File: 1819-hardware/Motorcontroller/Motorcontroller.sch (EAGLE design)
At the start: 33 parts, among them U1 GENERIC-SOIC8MSGEQ7N-FILTER, U2 GENERIC-SOIC8MSGEQ7N-FILTER, U3 GENERIC-SOIC8MSGEQ7N-FILTER

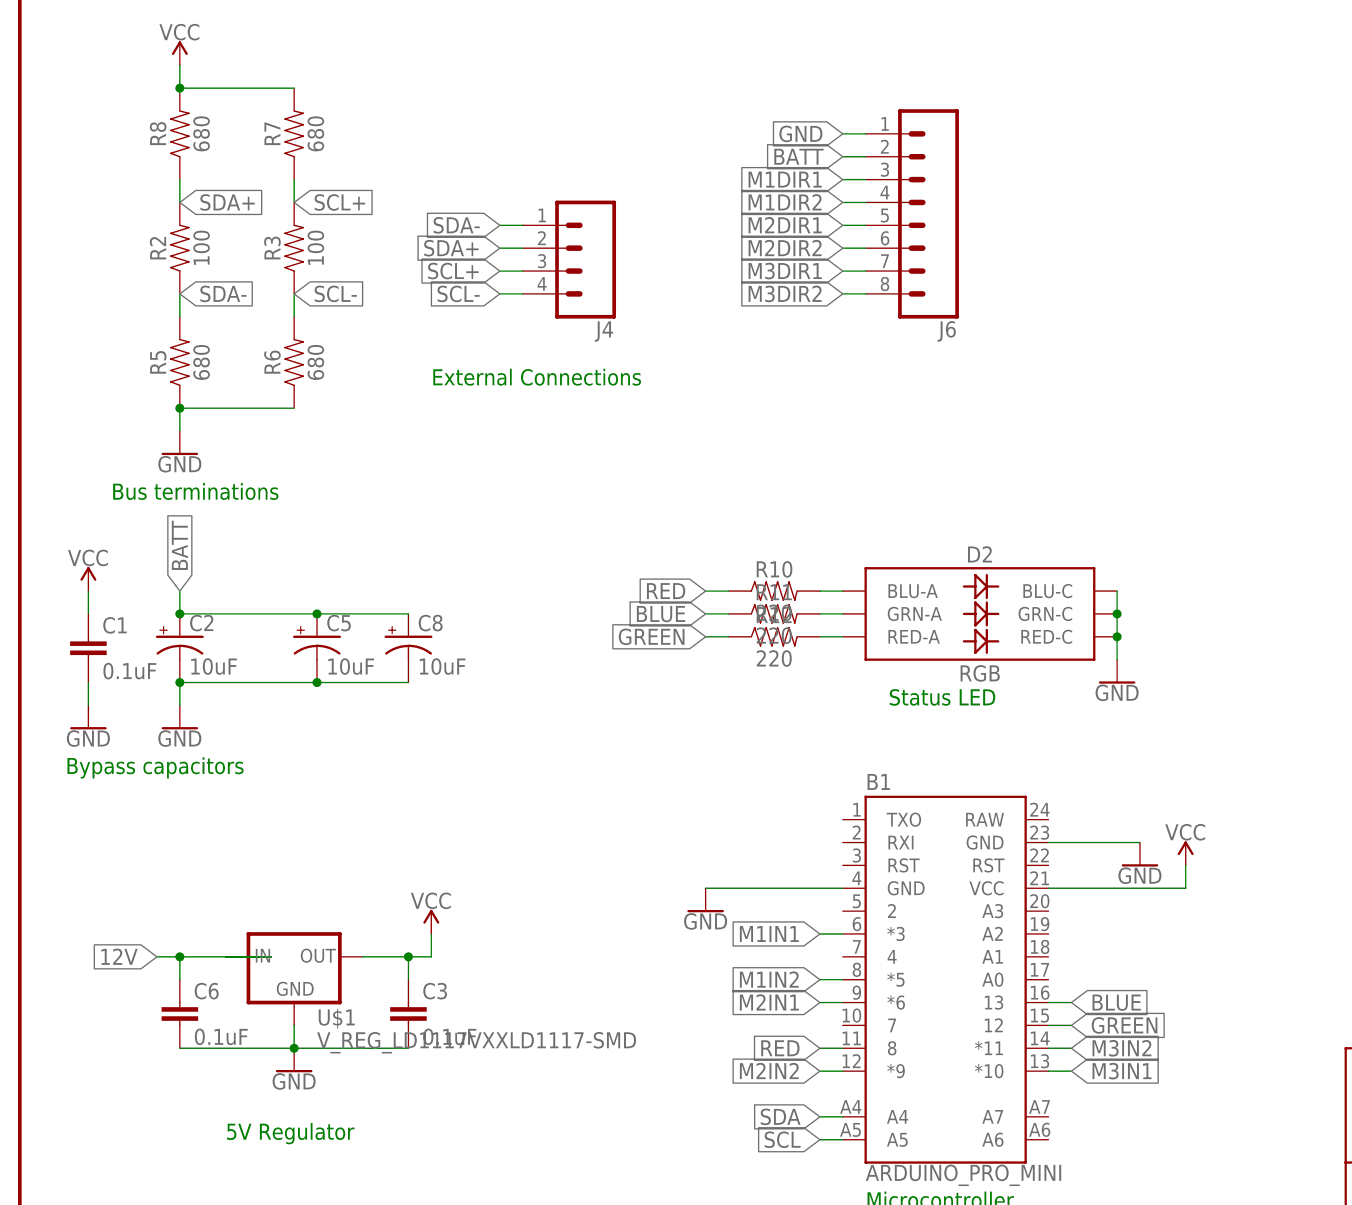
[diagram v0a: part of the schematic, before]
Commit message: routing of motorcontroller board files
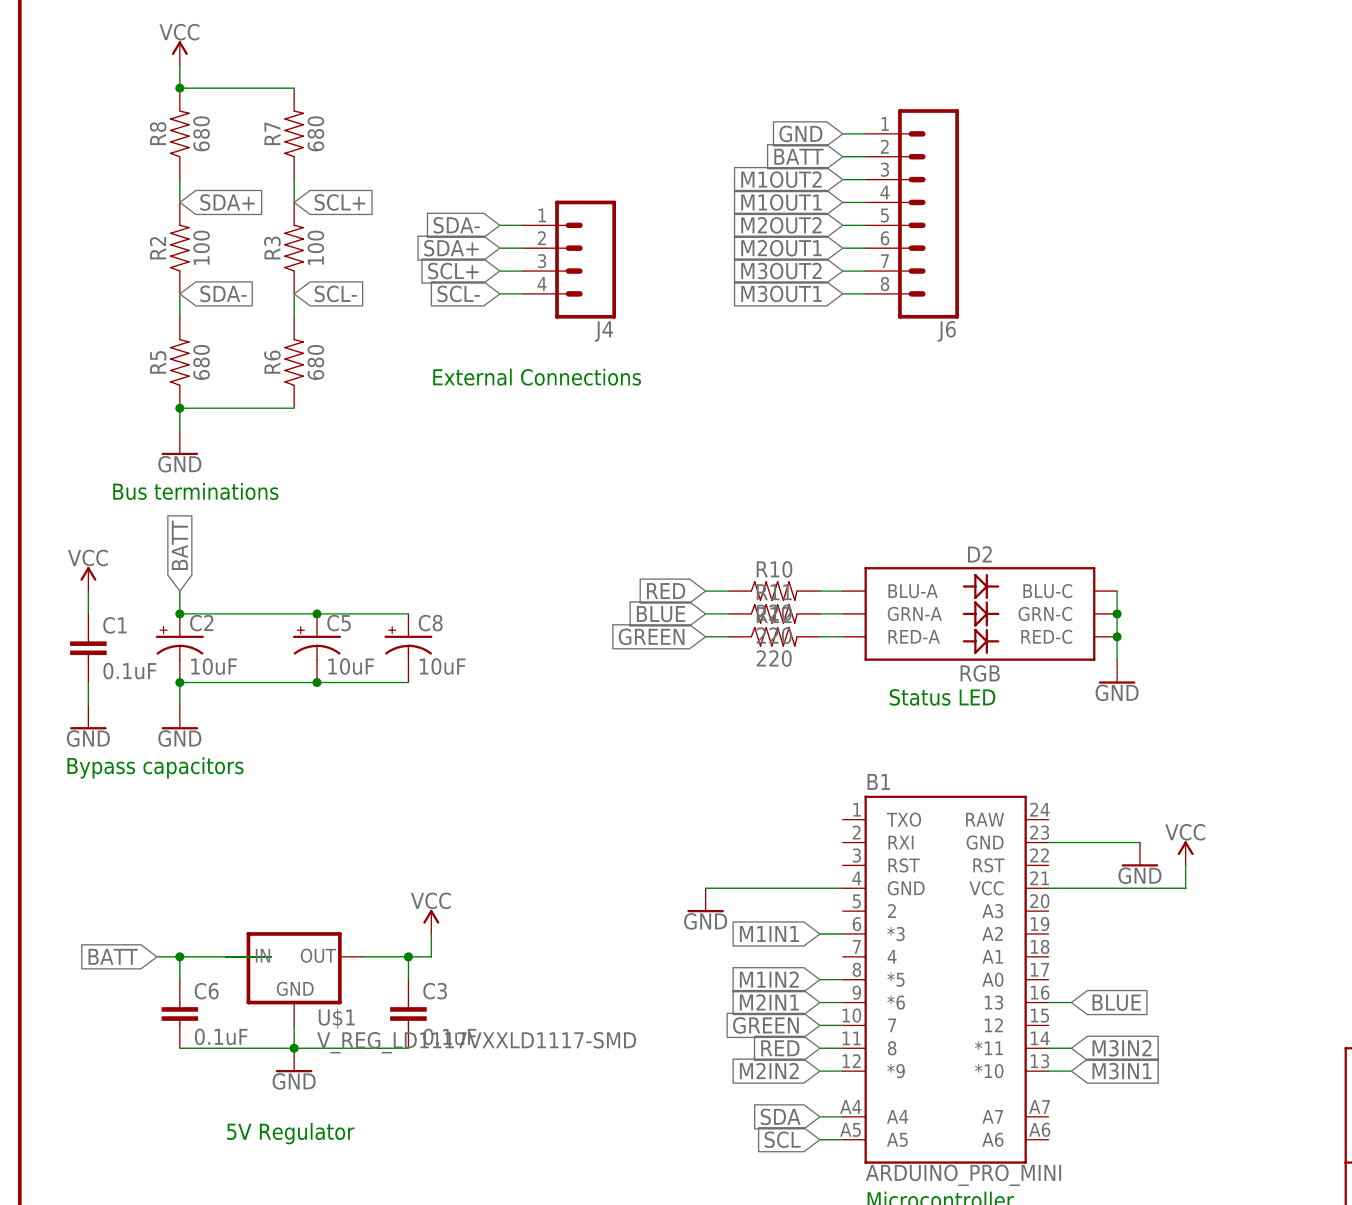
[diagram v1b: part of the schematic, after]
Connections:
- removed net 12V: C6.1, U$1.IN
- removed net M1DIR1: J6.3
- removed net M1DIR2: J6.4
- removed net M2DIR1: J6.5
- removed net M2DIR2: J6.6
- removed net M3DIR1: J6.7
- removed net M3DIR2: J6.8
- net BATT: now also C6.1, U$1.IN
- net GREEN: now also B1.7; no longer B1.12
- net M1OUT1: now also J6.4
- net M1OUT2: now also J6.3
- net M2OUT1: now also J6.6
- net M2OUT2: now also J6.5
- net M3OUT1: now also J6.8
- net M3OUT2: now also J6.7
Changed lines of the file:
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@@
-</segment>
-</net>
-<net name="12V" class="0">
-<segment>
-<pinref part="U$1" gate="G$1" pin="IN"/>
-<wire x1="22.86" y1="45.72" x2="27.94" y2="45.72" width="0.1524" layer="91"/>
-<wire x1="27.94" y1="45.72" x2="17.78" y2="45.72" width="0.1524" layer="91"/>
-<pinref part="C6" gate="G$1" pin="1"/>
-<wire x1="17.78" y1="45.72" x2="17.78" y2="43.18" width="0.1524" layer="91"/>
-<wire x1="17.78" y1="45.72" x2="15.24" y2="45.72" width="0.1524" layer="91"/>
-<junction x="17.78" y="45.72"/>
-<label x="15.24" y="45.72" size="1.778" layer="95" rot="R180" xref="yes"/>
 </segment>
 </net>
@@
 <net name="GREEN" class="0">
 <segment>
-<pinref part="B1" gate="G$1" pin="12"/>
-<wire x1="114.3" y1="38.1" x2="116.84" y2="38.1" width="0.1524" layer="91"/>
-<label x="116.84" y="38.1" size="1.778" layer="95" xref="yes"/>
-</segment>
-<segment>
 <pinref part="R12" gate="G$1" pin="1"/>
 <wire x1="78.74" y1="81.28" x2="76.2" y2="81.28" width="0.1524" layer="91"/>
 <label x="76.2" y="81.28" size="1.778" layer="95" rot="R180" xref="yes"/>
+</segment>
+<segment>
+<pinref part="B1" gate="G$1" pin="7"/>
+<wire x1="91.44" y1="38.1" x2="88.9" y2="38.1" width="0.1524" layer="91"/>
+<label x="88.9" y="38.1" size="1.778" layer="95" rot="R180" xref="yes"/>
 </segment>
 </net>
@@
 <label x="17.78" y="86.36" size="1.778" layer="95" rot="R90" xref="yes"/>
 </segment>
+<segment>
+<pinref part="U$1" gate="G$1" pin="IN"/>
+<wire x1="22.86" y1="45.72" x2="27.94" y2="45.72" width="0.1524" layer="91"/>
+<wire x1="27.94" y1="45.72" x2="17.78" y2="45.72" width="0.1524" layer="91"/>
+<pinref part="C6" gate="G$1" pin="1"/>
+<wire x1="17.78" y1="45.72" x2="17.78" y2="43.18" width="0.1524" layer="91"/>
+<wire x1="17.78" y1="45.72" x2="15.24" y2="45.72" width="0.1524" layer="91"/>
+<junction x="17.78" y="45.72"/>
+<label x="15.24" y="45.72" size="1.778" layer="95" rot="R180" xref="yes"/>
+</segment>
 </net>
 <net name="M1IN1" class="0">
@@
 <label x="198.12" y="167.64" size="1.778" layer="95" xref="yes"/>
 </segment>
+<segment>
+<pinref part="J6" gate="G$1" pin="3"/>
+<wire x1="93.98" y1="132.08" x2="91.44" y2="132.08" width="0.1524" layer="91"/>
+<label x="91.44" y="132.08" size="1.778" layer="95" rot="R180" xref="yes"/>
+</segment>
 </net>
 <net name="M1OUT1" class="0">
@@
 <label x="198.12" y="162.56" size="1.778" layer="95" xref="yes"/>
 </segment>
+<segment>
+<pinref part="J6" gate="G$1" pin="4"/>
+<wire x1="93.98" y1="129.54" x2="91.44" y2="129.54" width="0.1524" layer="91"/>
+<label x="91.44" y="129.54" size="1.778" layer="95" rot="R180" xref="yes"/>
+</segment>
 </net>
 <net name="N$1" class="0">
@@
 <label x="198.12" y="124.46" size="1.778" layer="95" xref="yes"/>
 </segment>
+<segment>
+<pinref part="J6" gate="G$1" pin="5"/>
+<wire x1="93.98" y1="127" x2="91.44" y2="127" width="0.1524" layer="91"/>
+<label x="91.44" y="127" size="1.778" layer="95" rot="R180" xref="yes"/>
+</segment>
 </net>
 <net name="M2OUT1" class="0">
@@
 <label x="198.12" y="119.38" size="1.778" layer="95" xref="yes"/>
 </segment>
+<segment>
+<pinref part="J6" gate="G$1" pin="6"/>
+<wire x1="93.98" y1="124.46" x2="91.44" y2="124.46" width="0.1524" layer="91"/>
+<label x="91.44" y="124.46" size="1.778" layer="95" rot="R180" xref="yes"/>
+</segment>
 </net>
 <net name="M3OUT2" class="0">
@@
 <label x="198.12" y="78.74" size="1.778" layer="95" xref="yes"/>
 </segment>
+<segment>
+<pinref part="J6" gate="G$1" pin="7"/>
+<wire x1="93.98" y1="121.92" x2="91.44" y2="121.92" width="0.1524" layer="91"/>
+<label x="91.44" y="121.92" size="1.778" layer="95" rot="R180" xref="yes"/>
+</segment>
 </net>
 <net name="M3OUT1" class="0">
@@
 <label x="198.12" y="73.66" size="1.778" layer="95" xref="yes"/>
 </segment>
-</net>
-<net name="M1DIR1" class="0">
-<segment>
-<pinref part="J6" gate="G$1" pin="3"/>
-<wire x1="93.98" y1="132.08" x2="91.44" y2="132.08" width="0.1524" layer="91"/>
-<label x="91.44" y="132.08" size="1.778" layer="95" rot="R180" xref="yes"/>
-</segment>
-</net>
-<net name="M1DIR2" class="0">
-<segment>
-<pinref part="J6" gate="G$1" pin="4"/>
-<wire x1="93.98" y1="129.54" x2="91.44" y2="129.54" width="0.1524" layer="91"/>
-<label x="91.44" y="129.54" size="1.778" layer="95" rot="R180" xref="yes"/>
-</segment>
-</net>
-<net name="M2DIR1" class="0">
-<segment>
-<pinref part="J6" gate="G$1" pin="5"/>
-<wire x1="93.98" y1="127" x2="91.44" y2="127" width="0.1524" layer="91"/>
-<label x="91.44" y="127" size="1.778" layer="95" rot="R180" xref="yes"/>
-</segment>
-</net>
-<net name="M2DIR2" class="0">
-<segment>
-<pinref part="J6" gate="G$1" pin="6"/>
-<wire x1="93.98" y1="124.46" x2="91.44" y2="124.46" width="0.1524" layer="91"/>
-<label x="91.44" y="124.46" size="1.778" layer="95" rot="R180" xref="yes"/>
-</segment>
-</net>
-<net name="M3DIR1" class="0">
-<segment>
-<pinref part="J6" gate="G$1" pin="7"/>
-<wire x1="93.98" y1="121.92" x2="91.44" y2="121.92" width="0.1524" layer="91"/>
-<label x="91.44" y="121.92" size="1.778" layer="95" rot="R180" xref="yes"/>
-</segment>
-</net>
-<net name="M3DIR2" class="0">
 <segment>
 <pinref part="J6" gate="G$1" pin="8"/>
